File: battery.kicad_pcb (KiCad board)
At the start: 2 copper layers, 27.9 x 25.4 mm, 21 parts, among them J1 Conn_01x04_Female, J2 Conn_02x05_Odd_Even, J3 Conn_02x03_Odd_Even, J4 Conn_01x06_Male, J5 Conn_01x02_Female, Q1 2N7002, Q2 Q_PMOS_GSD, Q3 Q_PMOS_GSD, U1 AP3428

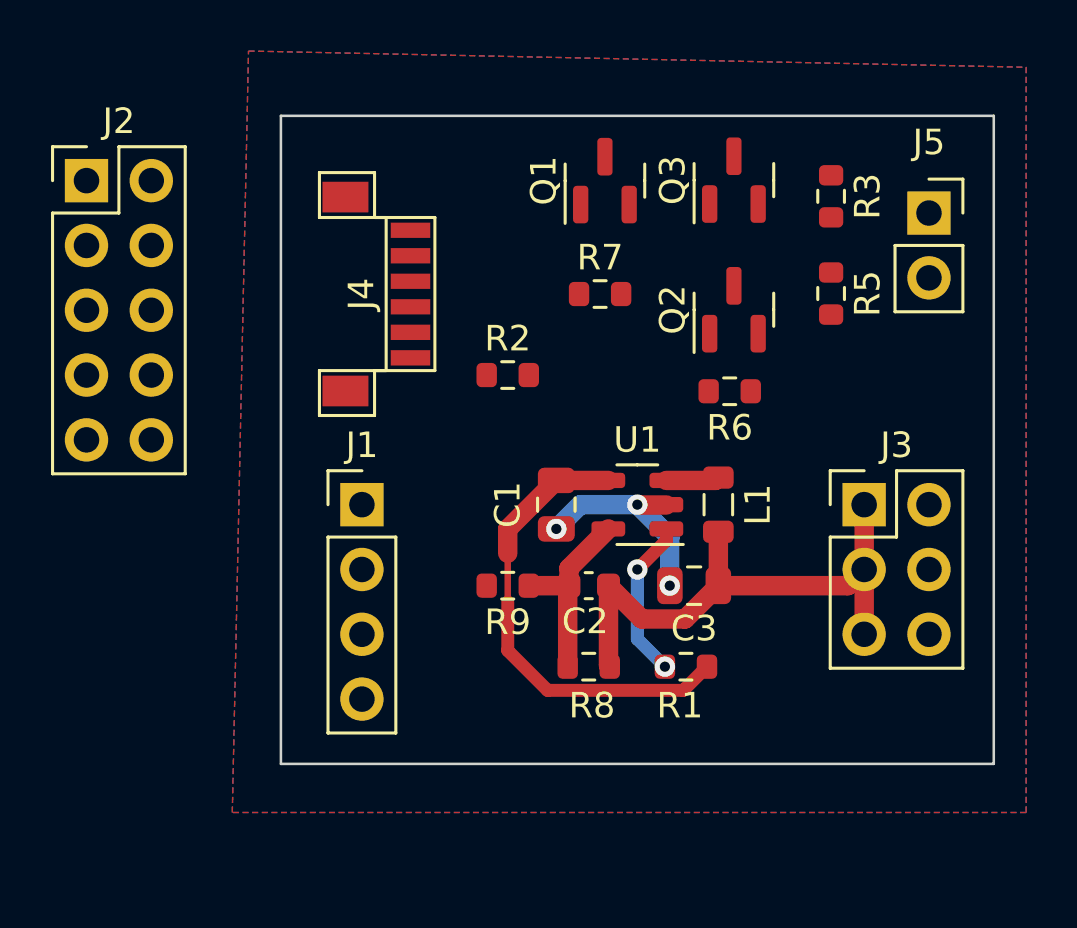
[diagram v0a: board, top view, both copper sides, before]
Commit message: High-side switch for solar cell.
Need to place the uC interconnect - maybe a surface-mount connector will
do
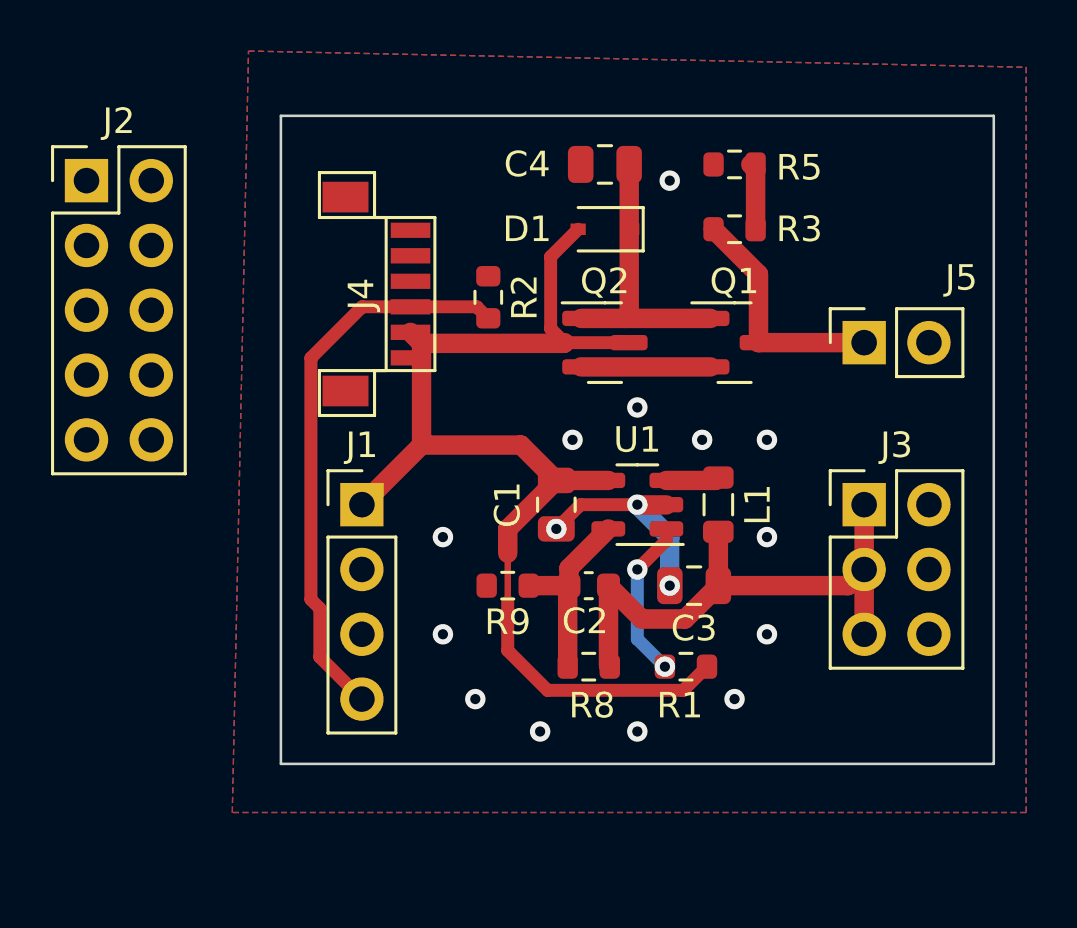
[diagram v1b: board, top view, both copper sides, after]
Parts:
- removed Q3: Q_PMOS_GSD, Package_TO_SOT_SMD:SOT-23
- removed R6, R7: 100k, Resistor_SMD:R_0603_1608Metric
- added C4: 10u, Capacitor_SMD:C_0805_2012Metric, F.Cu at (104.1, 88.3)
- added D1: D, Diode_SMD:D_SOD-323, F.Cu at (104.1, 90.8)
- Q1: value 2N7002 -> Q_NMOS_GSD
- Q2: value Q_PMOS_GSD -> Q_NMOS_GSD
- moved Q1 8.13 mm to (109.2, 95.2), turned to 0 degrees
- moved R5 6.32 mm to (109.2, 88.3), turned to 180 degrees
- moved J5 5.68 mm to (114.3, 95.2), turned to 90 degrees
- moved Q2 5.22 mm to (104.1, 95.2), turned to 0 degrees
- moved R3 4.00 mm to (109.2, 90.8), turned to 0 degrees
- moved R2 3.14 mm to (99.6, 93.5), turned to -90 degrees
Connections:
- Q1 pad 1: /solar_en -> Net-(Q1-Pad1)
- Q1 pad 2: GND -> Net-(Q1-Pad2)
- Q1 pad 3: Net-(Q1-Pad3) -> /solar
- Q2 pad 1: Net-(Q1-Pad3) -> Net-(Q1-Pad1)
- Q2 pad 2: Net-(Q3-Pad2) -> Net-(Q1-Pad2)
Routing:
- net +4V: track 18.3 -> 45.3 mm
- net /thermistor: track 0.00 -> 22.2 mm
- net Net-(Q1-Pad1): track 0.00 -> 11.2 mm
- net /solar: track 0.00 -> 9.32 mm
- net Net-(Q1-Pad2): track 0.00 -> 5.08 mm
- net /v_solar: track 0.00 -> 2.62 mm
- net GND: vias 3 -> 16

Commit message: Routed uC interconnect
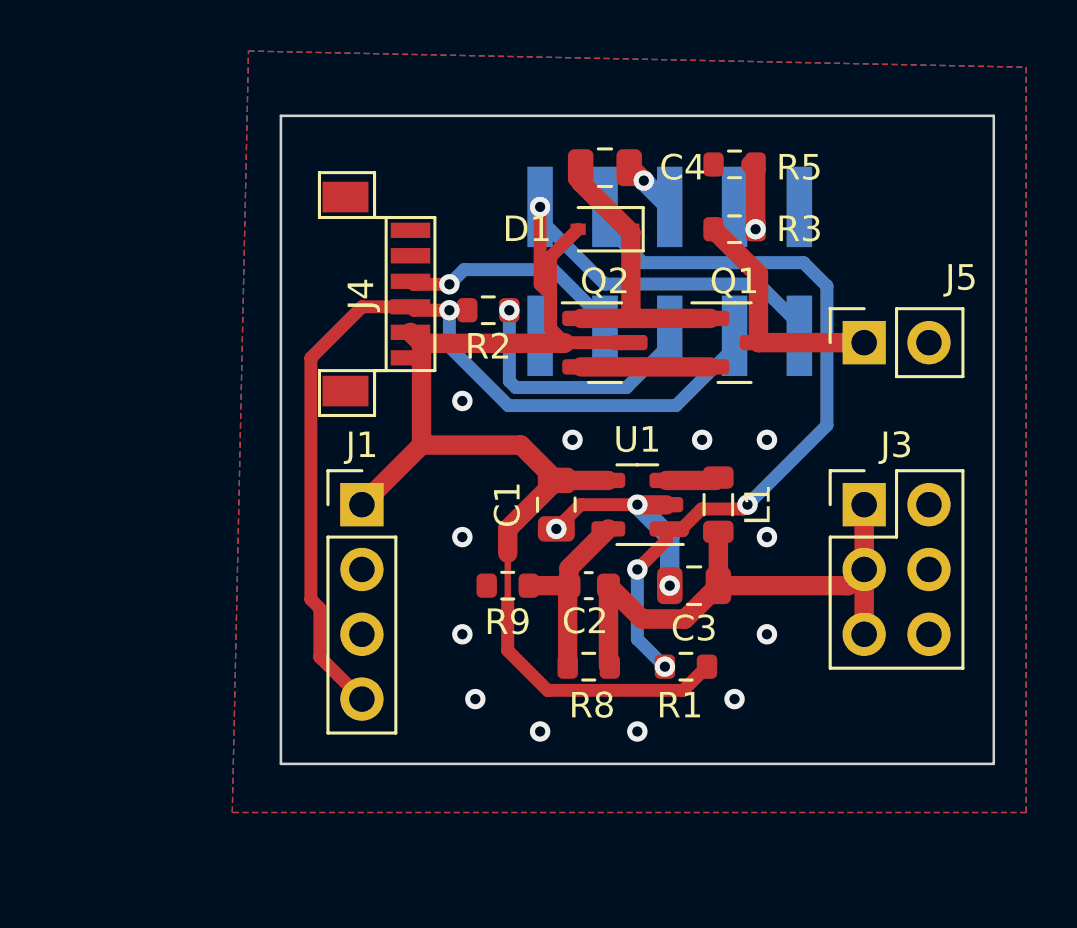
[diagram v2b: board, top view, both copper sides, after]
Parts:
- J2: footprint Connector_PinHeader_2.54mm:PinHeader_2x05_P2.54mm_Vertical -> Connector_PinHeader_2.54mm:PinHeader_2x05_P2.54mm_Vertical_SMD; moved to B.Cu
- moved J2 23.1 mm to (106.7, 92.5), turned to 90 degrees
- moved R2 0.51 mm to (99.6, 94.0), turned to 180 degrees
- moved C4 0.13 mm to (104.1, 88.4), turned to 0 degrees
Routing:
- net /3v3_en: track 6.32 -> 31.3 mm, vias 2 -> 3
- net +4V: track 45.3 -> 61.8 mm, vias 0 -> 1
- net /thermistor: track 22.2 -> 36.2 mm, vias 0 -> 1
- net /therm_en: track 0.00 -> 10.2 mm, vias 0 -> 1
- net /hdq: track 0.00 -> 9.31 mm, vias 0 -> 1
- net /solar_en: track 0.00 -> 2.24 mm, vias 0 -> 1
- net /v_solar: track 2.62 -> 3.83 mm, vias 0 -> 1
- net Net-(Q1-Pad1): track 11.2 -> 11.9 mm
- net GND: vias 16 -> 15

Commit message: Changed to single transistor for solar disconnect
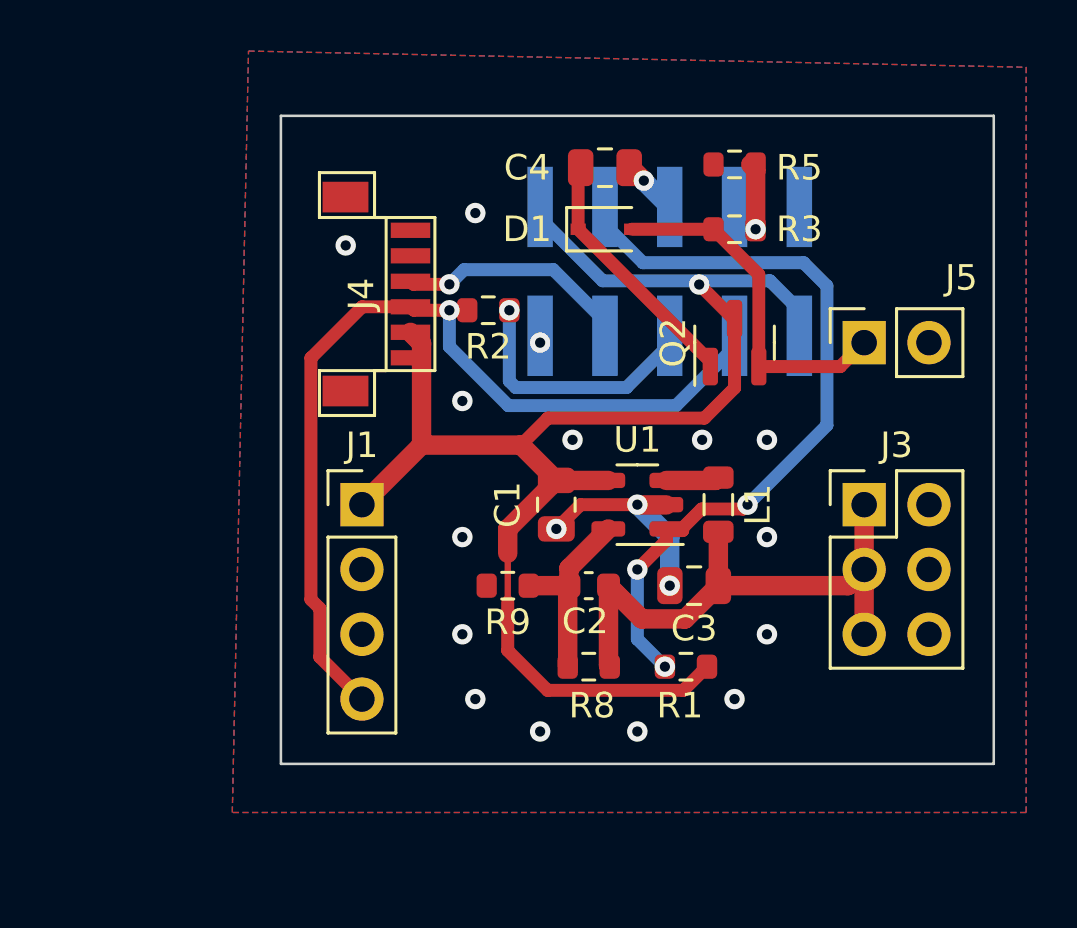
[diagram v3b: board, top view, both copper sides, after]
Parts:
- removed Q1: Q_NMOS_GSD, Package_TO_SOT_SMD:SOT-23
- moved Q2 5.08 mm to (109.2, 95.2), turned to 90 degrees
- turned D1 to 0 degrees
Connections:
- D1 pad 2: +4V -> /solar
- Q2 pad 2: Net-(Q1-Pad2) -> /solar
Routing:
- net Net-(Q1-Pad2): track 5.08 -> 0.00 mm
- net /solar: track 9.32 -> 13.8 mm
- net +4V: track 61.8 -> 59.1 mm
- net Net-(C4-Pad1): track 11.9 -> 9.98 mm
- net /3v3_en: track 31.3 -> 30.3 mm
- net GND: vias 15 -> 18

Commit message: Completed silkscreen, sent board to fab
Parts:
- added QR*****: qr, battery:qr, F.Cu at (116.2, 89.5)
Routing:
- net GND: vias 18 -> 17
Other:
- board text added: "+"
- board text added: "+3"
- board text added: "-"
- board text added: "Lipo manager v0.1 March 2022"
- board text added: "Thermistor"

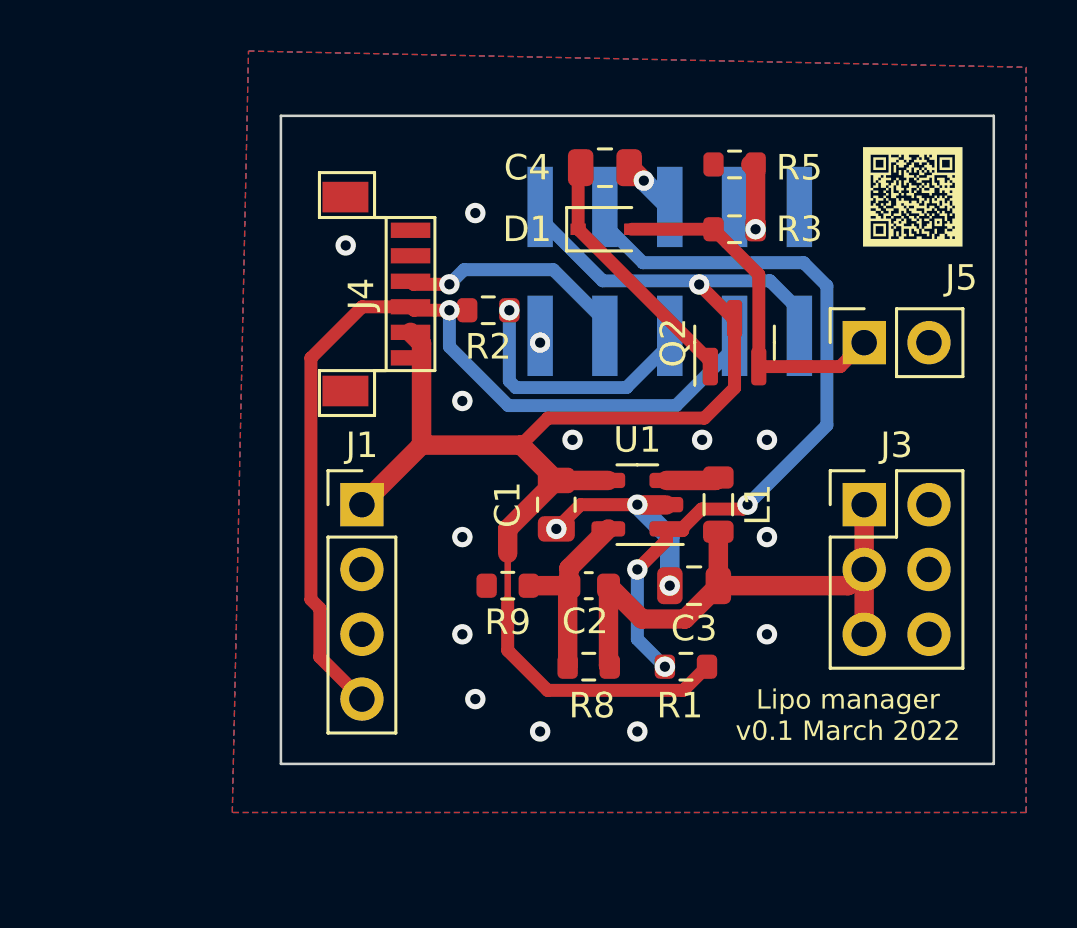
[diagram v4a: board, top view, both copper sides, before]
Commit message: Simplified board, switched to JST PH connector
Also upgraded to KiCad 7.0
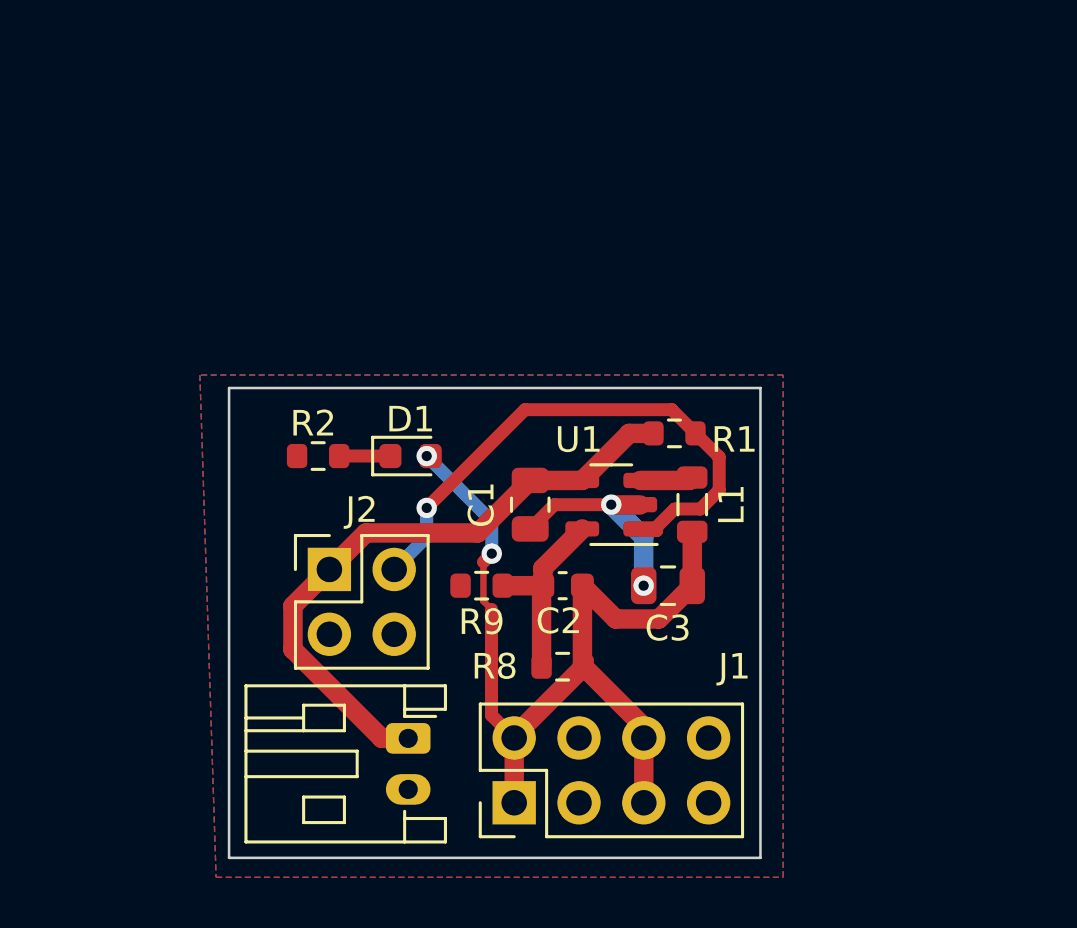
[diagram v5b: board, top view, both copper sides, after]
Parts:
- removed C4: 10u, Capacitor_SMD:C_0805_2012Metric
- removed J4: Conn_01x06_Male, battery:battery_connector
- removed J5: Conn_01x02_Female, Connector_PinSocket_2.54mm:PinSocket_1x02_P2.54mm_Vertical
- removed Q2: Q_NMOS_GSD, Package_TO_SOT_SMD:SOT-23
- removed QR*****: qr, battery:qr
- removed R3: 430k, Resistor_SMD:R_0603_1608Metric
- removed R5: 100k, Resistor_SMD:R_0603_1608Metric
- D1: value D -> LED; footprint Diode_SMD:D_SOD-323 -> LED_SMD:LED_0603_1608Metric
- J1: value Conn_01x04_Female -> Conn_02x04_Odd_Even; footprint Connector_PinHeader_2.54mm:PinHeader_1x04_P2.54mm_Vertical -> Connector_PinHeader_2.54mm:PinHeader_2x04_P2.54mm_Vertical
- J2: value Conn_02x05_Odd_Even -> Conn_02x02_Odd_Even; footprint Connector_PinHeader_2.54mm:PinHeader_2x05_P2.54mm_Vertical_SMD -> Connector_PinHeader_2.54mm:PinHeader_2x02_P2.54mm_Vertical; moved to F.Cu
- J3: value Conn_02x03_Odd_Even -> Conn_01x02_Pin; footprint Connector_PinHeader_2.54mm:PinHeader_2x03_P2.54mm_Vertical -> Connector_JST:JST_PH_S2B-PH-K_1x02_P2.00mm_Horizontal
- R2: value 10k -> 200
- moved J3 20.1 mm to (96.4, 110.8), turned to -90 degrees
- moved J2 17.7 mm to (93.3, 104.1), turned to 0 degrees
- moved J1 13.1 mm to (100.6, 113.3), turned to 90 degrees
- moved D1 11.7 mm to (96.5, 99.7)
- moved R1 9.16 mm to (106.9, 98.8), turned to 180 degrees
- moved R2 8.78 mm to (92.9, 99.7)
- moved C3 1.02 mm to (106.6, 104.8)
- moved C1 1.02 mm to (101.2, 101.6)
- moved C2 1.02 mm to (102.5, 104.8)
- moved L1 1.02 mm to (107.6, 101.6)
- moved R8 1.02 mm to (102.5, 108.0)
- moved R9 1.02 mm to (99.3, 104.8)
- moved U1 1.02 mm to (104.4, 101.6)
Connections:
- C2 pad 1: +3V3 -> +3.3V
- C3 pad 1: +3V3 -> +3.3V
- D1 pad 1: Net-(C4-Pad1) -> Net-(D1-K)
- D1 pad 2: /solar -> +3.3V
- J1 pad 1: +4V -> +3.3V
- J1 pad 2: GND -> +3.3V
- J1 pad 4: /thermistor -> GND
- J2 pad 2: GND -> /3v3_en
- J2 pad 3: /thermistor -> GND
- J2 pad 4: /v_solar -> GND
- J3 pad 1: +3V3 -> +4V
- L1 pad 2: +3V3 -> +3.3V
- R2 pad 1: /therm_en -> Net-(D1-K)
- R2 pad 2: /thermistor -> GND
- R8 pad 1: +3V3 -> +3.3V
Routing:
- net +3.3V: track 0.00 -> 36.4 mm, vias 0 -> 2
- net /thermistor: track 36.2 -> 0.00 mm, vias 1 -> 0
- net +4V: track 59.1 -> 24.6 mm, vias 1 -> 0
- net +3V3: track 21.8 -> 0.00 mm
- net /solar: track 13.8 -> 0.00 mm
- net /therm_en: track 10.2 -> 0.00 mm, vias 1 -> 0
- net Net-(C4-Pad1): track 9.98 -> 0.00 mm
- net /hdq: track 9.31 -> 0.00 mm, vias 1 -> 0
- net /3v3_en: track 30.3 -> 23.1 mm, vias 3 -> 1
- net /v_solar: track 3.83 -> 0.00 mm, vias 1 -> 0
- net /solar_en: track 2.24 -> 0.00 mm, vias 1 -> 0
- net Net-(D1-K): track 0.00 -> 2.01 mm
- net GND: vias 17 -> 2
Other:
- board size 27.9 x 25.4 mm -> 20.8 x 18.4 mm
- board text added: "+ -"
- board text added: "3.3V Regulator Marshal Horn March 2023"
- board text added: "3V Out - + - +"
- board text added: "Aux Pwr"
- board text added: "Battery"
- board text added: "En Gnd"
- board text removed: "+"
- board text removed: "+3"
- board text removed: "-"
- board text removed: "Lipo manager v0.1 March 2022"
- board text removed: "Thermistor"

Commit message: Silkscreen adjustements
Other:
- board text added: "4V"
- board text added: "En"
- board text added: "Gnd"
- board text removed: "Aux Pwr"
- board text removed: "En Gnd"
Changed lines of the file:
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@@
     (property "ki_keywords" "connector")
     (attr through_hole)
-    (fp_text reference "J3" (at 2.905 4.355) (layer "B.SilkS")
+    (fp_text reference "J3" (at 2.905 4.355) (layer "B.SilkS") hide
         (effects (font (size 1 1) (thickness 0.15)) (justify mirror))
     )
@@
     (fp_line (start 3.95 6.25) (end 3.95 -1.35)
       (stroke (width 0.1) (type solid)) (layer "F.Fab"))
-    (pad "1" thru_hole roundrect (at 0 0 270) (size 1.2 1.75) (drill 0.75) (layers "*.Cu" "*.Mask") (roundrect_rratio 0.208333)
+    (pad "1" thru_hole roundrect (at 0 0 270) (size 1.2 1.75) (drill 0.75) (layers "*.Cu" "*.Mask") (roundrect_rratio 0.2083333333)
       (net 1 "+4V") (pinfunction "Pin_1") (pintype "passive"))
     (pad "2" thru_hole oval (at 2 0 270) (size 1.2 1.75) (drill 0.75) (layers "*.Cu" "*.Mask")
@@
   (gr_rect (start 89.408 97.028) (end 110.236 115.443)
     (stroke (width 0.1) (type solid)) (fill none) (layer "Edge.Cuts"))
-  (gr_text "Battery" (at 95.25 109.855) (layer "B.SilkS")
-    (effects (font (size 1 1) (thickness 0.15)) (justify left bottom mirror))
-  )
-  (gr_text "+\n-" (at 91.44 106.68) (layer "B.SilkS")
-    (effects (font (size 1 1) (thickness 0.15)) (justify left bottom mirror))
-  )
-  (gr_text "Aux Pwr" (at 95.885 102.87) (layer "B.SilkS")
+  (gr_text "Gnd" (at 99.695 107.315) (layer "B.SilkS")
+    (effects (font (size 1 1) (thickness 0.15)) (justify left bottom mirror))
+  )
+  (gr_text "Battery" (at 92.71 109.22 90) (layer "B.SilkS")
+    (effects (font (size 1 1) (thickness 0.15)) (justify left bottom mirror))
+  )
+  (gr_text "Gnd" (at 92.075 107.315) (layer "B.SilkS")
+    (effects (font (size 1 1) (thickness 0.15)) (justify left bottom mirror))
+  )
+  (gr_text "4V" (at 92.075 104.775) (layer "B.SilkS")
     (effects (font (size 1 1) (thickness 0.15)) (justify left bottom mirror))
   )
@@
     (effects (font (size 1 1) (thickness 0.15)) (justify left bottom mirror))
   )
-  (gr_text "En\nGnd" (at 97.155 106.68) (layer "B.SilkS")
+  (gr_text "En" (at 97.155 104.775) (layer "B.SilkS")
     (effects (font (size 1 1) (thickness 0.15)) (justify right bottom mirror))
   )
